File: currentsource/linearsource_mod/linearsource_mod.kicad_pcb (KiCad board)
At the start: 2 copper layers, 50 x 20 mm, 16 parts, among them P1 CONN_01X04, P2 CONN_01X04, Q1 Q_NMOS_DGS, Q2 BC849, U1 LM358

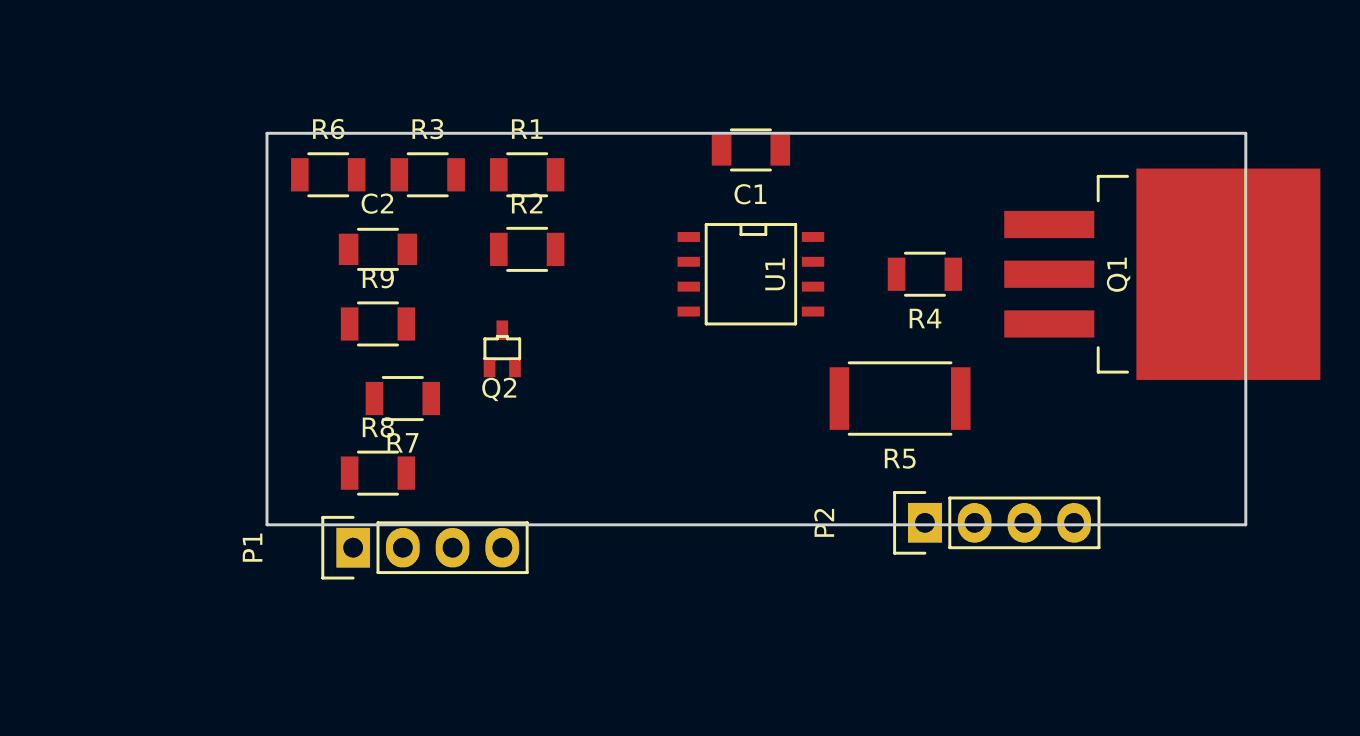
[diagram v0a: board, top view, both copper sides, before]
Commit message: currentsource: Prettify schematic for v2
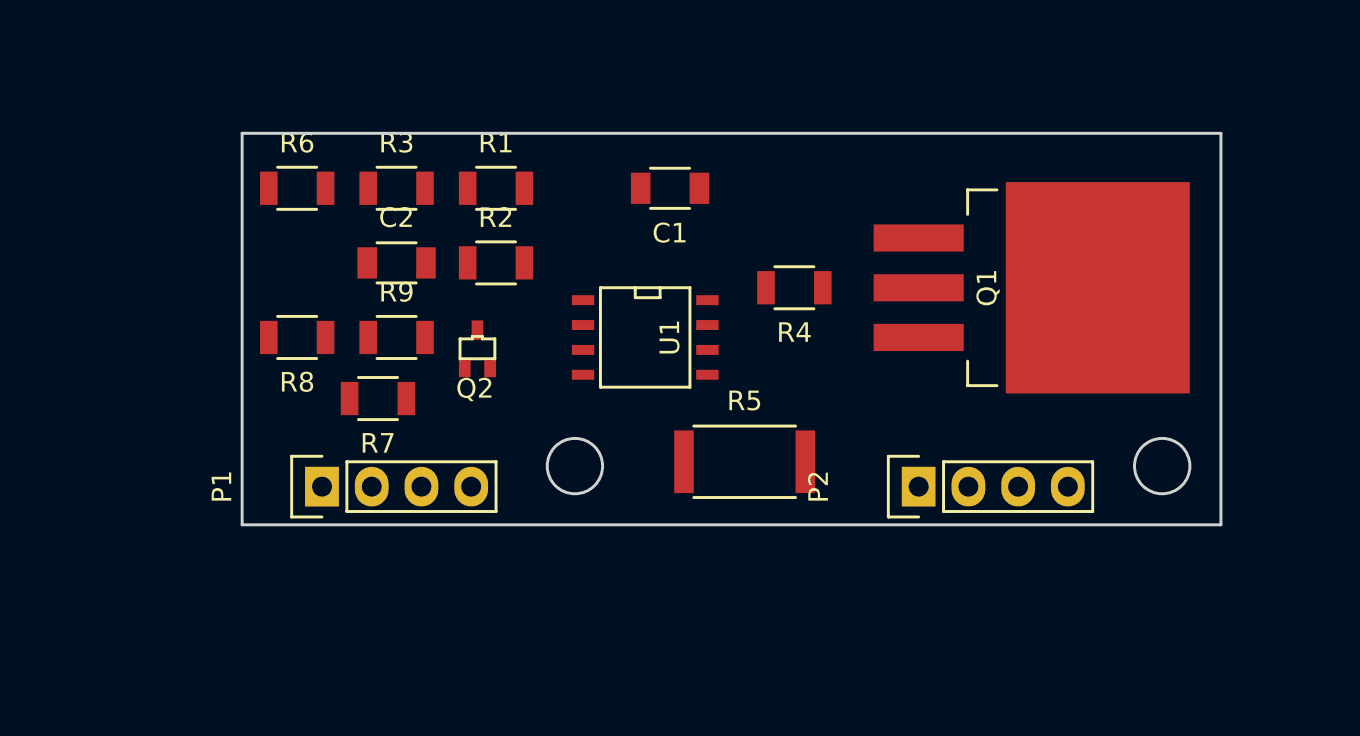
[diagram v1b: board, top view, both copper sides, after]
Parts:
- moved R5 8.57 mm to (172.4, 85.8), turned to 0 degrees
- moved R8 8.07 mm to (149.5, 79.4), turned to 180 degrees
- moved Q1 6.71 mm to (181.3, 76.9)
- moved R4 6.71 mm to (174.9, 76.9)
- moved U1 6.29 mm to (167.3, 79.4)
- moved C1 4.57 mm to (168.6, 71.8)
- moved P1 3.50 mm to (150.8, 87.0)
- moved P2 1.88 mm to (181.3, 87.0)
- moved R1 1.73 mm to (159.7, 71.8)
- moved R2 1.73 mm to (159.7, 75.6)
- moved R3 1.73 mm to (154.6, 71.8)
- moved R6 1.73 mm to (149.5, 71.8)
- moved Q2 1.27 mm to (158.8, 80.0)
- moved R7 1.27 mm to (153.7, 82.5)
- moved R9 1.17 mm to (154.6, 79.4)
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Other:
- outline, holes or cut-outs redrawn
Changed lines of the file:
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@@
     (links 28)
     (no_connects 28)
-    (area 147.924999 68.924999 198.075001 89.075001)
+    (area 146.654999 68.924999 196.805001 89.075001)
     (thickness 1.6)
-    (drawings 4)
+    (drawings 8)
     (tracks 0)
     (zones 0)
@@
     (pad_drill 0.762)
     (pad_to_mask_clearance 0.2)
-    (aux_axis_origin 0 0)
-    (grid_origin 147 68)
+    (aux_axis_origin 145.73 68)
+    (grid_origin 145.73 68)
     (visible_elements FFFEFF7F)
     (pcbplotparams
@@
   )
   (module TO_SOT_Packages_SMD:SOT-323 (layer F.Cu)
-    (at 160.02 80.01 180)
+    (at 158.75 80.01 180)
     (tags "SMD SOT")
     (attr smd)
@@
   )
   (module Capacitors_SMD:C_1206 (layer F.Cu)
-    (at 172.72 69.85 180)
+    (at 168.59 71.81 180)
     (descr "Capacitor SMD 1206, reflow soldering, AVX (see smccp.pdf)")
     (tags "capacitor 1206")
@@
   )
   (module Capacitors_SMD:C_1206 (layer F.Cu)
-    (at 153.67 74.93)
+    (at 154.62 75.62)
     (descr "Capacitor SMD 1206, reflow soldering, AVX (see smccp.pdf)")
     (tags "capacitor 1206")
@@
   )
   (module Pin_Headers:Pin_Header_Straight_1x04 (layer F.Cu)
-    (at 152.4 90.17 90)
+    (at 150.81 87.05 90)
     (descr "Through hole pin header")
     (tags "pin header")
@@
   )
   (module Pin_Headers:Pin_Header_Straight_1x04 (layer F.Cu)
-    (at 181.61 88.9 90)
+    (at 181.29 87.05 90)
     (descr "Through hole pin header")
     (tags "pin header")
@@
   )
   (module TO_SOT_Packages_SMD:TO-263-3Lead (layer F.Cu)
-    (at 187.96 76.2)
+    (at 181.29 76.89)
     (descr "D2PAK / TO-263 3-lead smd package")
     (tags "D2PAK D2PAK-3 TO-263AB TO-263")
@@
   )
   (module Resistors_SMD:R_1206 (layer F.Cu)
-    (at 161.29 71.12)
+    (at 159.7 71.81)
     (descr "Resistor SMD 1206, reflow soldering, Vishay (see dcrcw.pdf)")
     (tags "resistor 1206")
@@
   )
   (module Resistors_SMD:R_1206 (layer F.Cu)
-    (at 161.29 74.93)
+    (at 159.7 75.62)
     (descr "Resistor SMD 1206, reflow soldering, Vishay (see dcrcw.pdf)")
     (tags "resistor 1206")
@@
   )
   (module Resistors_SMD:R_1206 (layer F.Cu)
-    (at 156.21 71.12)
+    (at 154.62 71.81)
     (descr "Resistor SMD 1206, reflow soldering, Vishay (see dcrcw.pdf)")
     (tags "resistor 1206")
@@
   )
   (module Resistors_SMD:R_1206 (layer F.Cu)
-    (at 181.61 76.2 180)
+    (at 174.94 76.89 180)
     (descr "Resistor SMD 1206, reflow soldering, Vishay (see dcrcw.pdf)")
     (tags "resistor 1206")
@@
   )
   (module Resistors_SMD:R_1206 (layer F.Cu)
-    (at 151.13 71.12)
+    (at 149.54 71.81)
     (descr "Resistor SMD 1206, reflow soldering, Vishay (see dcrcw.pdf)")
     (tags "resistor 1206")
@@
   )
   (module Resistors_SMD:R_1206 (layer F.Cu)
-    (at 154.94 82.55 180)
+    (at 153.67 82.55 180)
     (descr "Resistor SMD 1206, reflow soldering, Vishay (see dcrcw.pdf)")
     (tags "resistor 1206")
@@
   )
   (module Resistors_SMD:R_1206 (layer F.Cu)
-    (at 153.67 86.36)
-    (descr "Resistor SMD 1206, reflow soldering, Vishay (see dcrcw.pdf)")
-    (tags "resistor 1206")
-    (attr smd)
-    (fp_text reference R8 (at 0 -2.3) (layer F.SilkS)
-      (effects (font (size 1 1) (thickness 0.15)))
-    )
-    (fp_text value 100k (at 0 2.3) (layer F.Fab)
-      (effects (font (size 1 1) (thickness 0.15)))
-    )
-    (fp_line (start -2.2 -1.2) (end 2.2 -1.2) (layer F.CrtYd) (width 0.05))
-    (fp_line (start -2.2 1.2) (end 2.2 1.2) (layer F.CrtYd) (width 0.05))
-    (fp_line (start -2.2 -1.2) (end -2.2 1.2) (layer F.CrtYd) (width 0.05))
-    (fp_line (start 2.2 -1.2) (end 2.2 1.2) (layer F.CrtYd) (width 0.05))
-    (fp_line (start 1 1.075) (end -1 1.075) (layer F.SilkS) (width 0.15))
-    (fp_line (start -1 -1.075) (end 1 -1.075) (layer F.SilkS) (width 0.15))
-    (pad 1 smd rect (at -1.45 0) (size 0.9 1.7) (layers F.Cu F.Paste F.Mask)
+    (at 149.54 79.43 180)
+    (descr "Resistor SMD 1206, reflow soldering, Vishay (see dcrcw.pdf)")
+    (tags "resistor 1206")
+    (attr smd)
+    (fp_text reference R8 (at 0 -2.3 180) (layer F.SilkS)
+      (effects (font (size 1 1) (thickness 0.15)))
+    )
+    (fp_text value 100k (at 0 2.3 180) (layer F.Fab)
+      (effects (font (size 1 1) (thickness 0.15)))
+    )
+    (fp_line (start -2.2 -1.2) (end 2.2 -1.2) (layer F.CrtYd) (width 0.05))
+    (fp_line (start -2.2 1.2) (end 2.2 1.2) (layer F.CrtYd) (width 0.05))
+    (fp_line (start -2.2 -1.2) (end -2.2 1.2) (layer F.CrtYd) (width 0.05))
+    (fp_line (start 2.2 -1.2) (end 2.2 1.2) (layer F.CrtYd) (width 0.05))
+    (fp_line (start 1 1.075) (end -1 1.075) (layer F.SilkS) (width 0.15))
+    (fp_line (start -1 -1.075) (end 1 -1.075) (layer F.SilkS) (width 0.15))
+    (pad 1 smd rect (at -1.45 0 180) (size 0.9 1.7) (layers F.Cu F.Paste F.Mask)
       (net 5 /I_target))
-    (pad 2 smd rect (at 1.45 0) (size 0.9 1.7) (layers F.Cu F.Paste F.Mask)
+    (pad 2 smd rect (at 1.45 0 180) (size 0.9 1.7) (layers F.Cu F.Paste F.Mask)
       (net 7 I_set))
     (model Resistors_SMD.3dshapes/R_1206.wrl
@@
   )
   (module Resistors_SMD:R_1206 (layer F.Cu)
-    (at 153.67 78.74)
+    (at 154.62 79.43)
     (descr "Resistor SMD 1206, reflow soldering, Vishay (see dcrcw.pdf)")
     (tags "resistor 1206")
@@
   )
   (module SMD_Packages:SOIC-8-N (layer F.Cu)
-    (at 172.72 76.2 270)
+    (at 167.32 79.43 270)
     (descr "Module Narrow CMS SOJ 8 pins large")
     (tags "CMS SOJ")
@@
   )
   (module Resistors_SMD:R_2512 (layer F.Cu)
-    (at 180.34 82.55 180)
+    (at 172.4 85.78)
     (descr "Resistor SMD 2512, reflow soldering, Vishay (see dcrcw.pdf)")
     (tags "resistor 2512")
     (attr smd)
-    (fp_text reference R5 (at 0 -3.1 180) (layer F.SilkS)
-      (effects (font (size 1 1) (thickness 0.15)))
-    )
-    (fp_text value 0.1 (at 0 3.1 180) (layer F.Fab)
+    (fp_text reference R5 (at 0 -3.1) (layer F.SilkS)
+      (effects (font (size 1 1) (thickness 0.15)))
+    )
+    (fp_text value 0.1 (at 0 3.1) (layer F.Fab)
       (effects (font (size 1 1) (thickness 0.15)))
     )
@@
     (fp_line (start 2.6 1.825) (end -2.6 1.825) (layer F.SilkS) (width 0.15))
     (fp_line (start -2.6 -1.825) (end 2.6 -1.825) (layer F.SilkS) (width 0.15))
-    (pad 1 smd rect (at -3.1 0 180) (size 1 3.2) (layers F.Cu F.Paste F.Mask)
+    (pad 1 smd rect (at -3.1 0) (size 1 3.2) (layers F.Cu F.Paste F.Mask)
       (net 12 I_sense))
-    (pad 2 smd rect (at 3.1 0 180) (size 1 3.2) (layers F.Cu F.Paste F.Mask)
+    (pad 2 smd rect (at 3.1 0) (size 1 3.2) (layers F.Cu F.Paste F.Mask)
       (net 8 GNDPWR))
     (model Resistors_SMD.3dshapes/R_2512.wrl
@@
     )
   )
-  (gr_line (start 148 89) (end 148 69) (angle 90) (layer Edge.Cuts) (width 0.15))
-  (gr_line (start 198 89) (end 148 89) (angle 90) (layer Edge.Cuts) (width 0.15))
-  (gr_line (start 198 69) (end 198 89) (angle 90) (layer Edge.Cuts) (width 0.15))
-  (gr_line (start 148 69) (end 198 69) (angle 90) (layer Edge.Cuts) (width 0.15))
+  (gr_circle (center 193.73 86) (end 194.73 85) (layer Edge.Cuts) (width 0.15))
+  (gr_circle (center 163.73 86) (end 164.73 85) (layer Edge.Cuts) (width 0.15))
+  (dimension 20 (width 0.3) (layer Eco2.User)
+    (gr_text "20.000 mm" (at 206.08 79 90) (layer Eco2.User)
+      (effects (font (size 1.5 1.5) (thickness 0.3)))
+    )
+    (feature1 (pts (xy 197.73 69) (xy 207.43 69)))
+    (feature2 (pts (xy 197.73 89) (xy 207.43 89)))
+    (crossbar (pts (xy 204.73 89) (xy 204.73 69)))
+    (arrow1a (pts (xy 204.73 69) (xy 205.316421 70.126504)))
+    (arrow1b (pts (xy 204.73 69) (xy 204.143579 70.126504)))
+    (arrow2a (pts (xy 204.73 89) (xy 205.316421 87.873496)))
+    (arrow2b (pts (xy 204.73 89) (xy 204.143579 87.873496)))
+  )
+  (dimension 50 (width 0.3) (layer Eco2.User)
+    (gr_text "50.000 mm" (at 171.73 95.35) (layer Eco2.User)
+      (effects (font (size 1.5 1.5) (thickness 0.3)))
+    )
+    (feature1 (pts (xy 146.73 90) (xy 146.73 96.7)))
+    (feature2 (pts (xy 196.73 90) (xy 196.73 96.7)))
+    (crossbar (pts (xy 196.73 94) (xy 146.73 94)))
+    (arrow1a (pts (xy 146.73 94) (xy 147.856504 93.413579)))
+    (arrow1b (pts (xy 146.73 94) (xy 147.856504 94.586421)))
+    (arrow2a (pts (xy 196.73 94) (xy 195.603496 93.413579)))
+    (arrow2b (pts (xy 196.73 94) (xy 195.603496 94.586421)))
+  )
+  (gr_line (start 146.73 89) (end 146.73 69) (angle 90) (layer Edge.Cuts) (width 0.15))
+  (gr_line (start 196.73 89) (end 146.73 89) (angle 90) (layer Edge.Cuts) (width 0.15))
+  (gr_line (start 196.73 69) (end 196.73 89) (angle 90) (layer Edge.Cuts) (width 0.15))
+  (gr_line (start 146.73 69) (end 196.73 69) (angle 90) (layer Edge.Cuts) (width 0.15))
 )

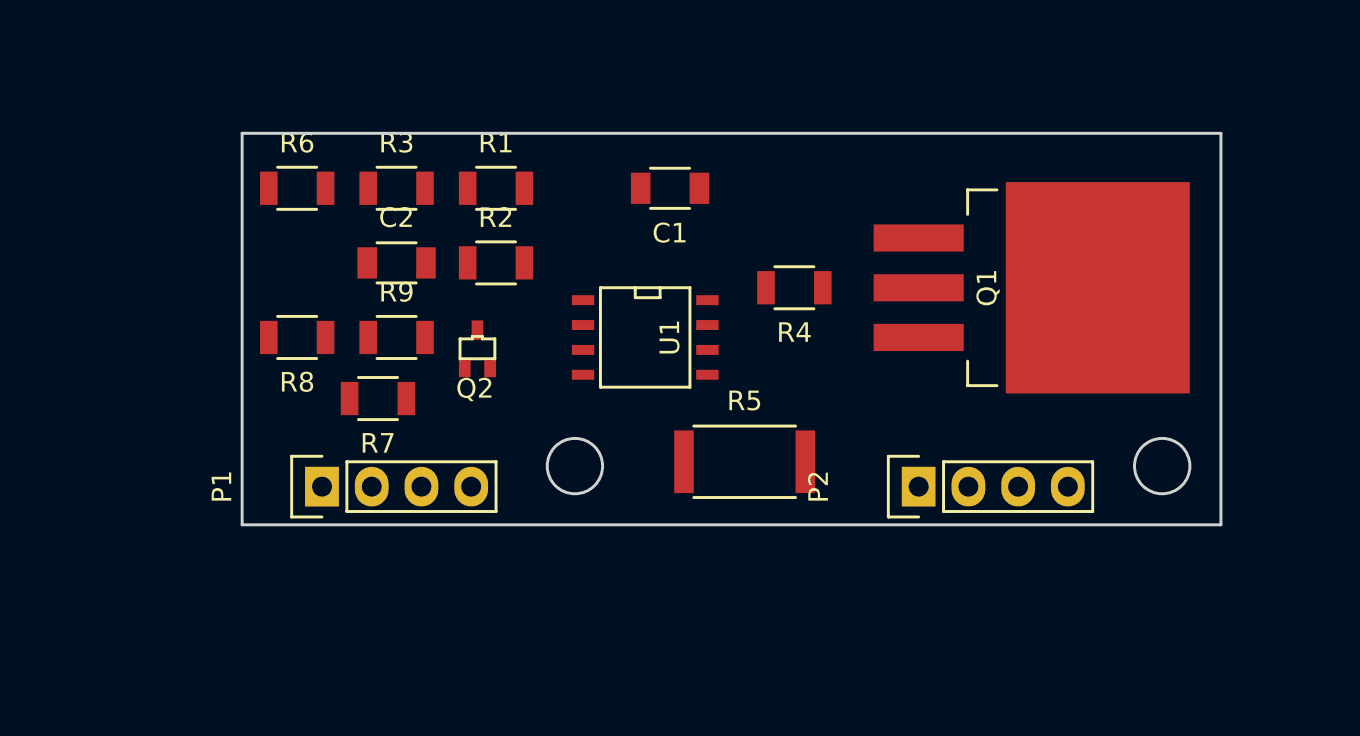
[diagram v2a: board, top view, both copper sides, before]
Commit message: currentsource: Start of routing tracks
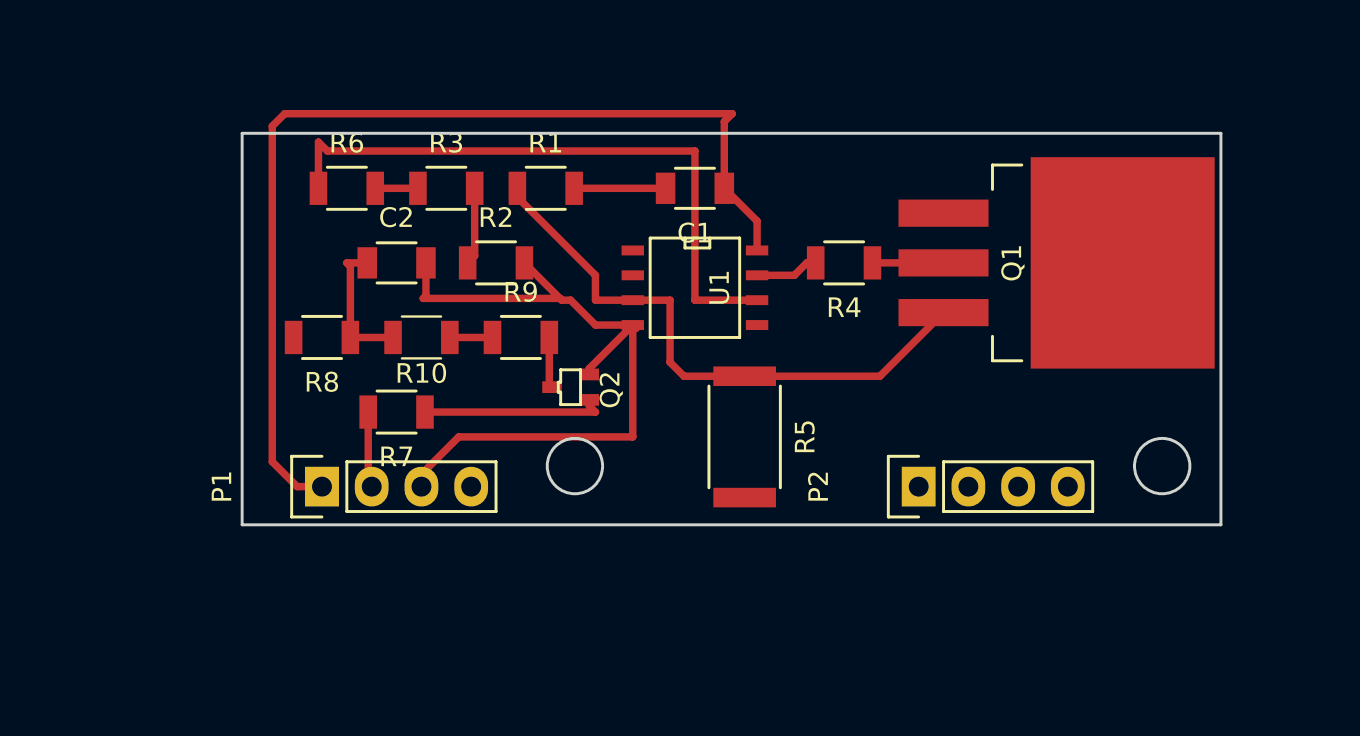
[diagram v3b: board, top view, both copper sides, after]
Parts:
- added R10: 100k, Resistors_SMD:R_1206, F.Cu at (155.9, 79.4)
- Q1: value Q_NMOS_DGS -> PSMN017-30BL
- moved R9 6.35 mm to (161.0, 79.4)
- moved Q2 5.15 mm to (163.5, 82.0), turned to 270 degrees
- moved U1 3.59 mm to (169.9, 76.9)
- moved R4 2.84 mm to (177.5, 75.6)
- moved R1 2.54 mm to (162.2, 71.8)
- moved R6 2.54 mm to (152.1, 71.8)
- moved R3 2.54 mm to (157.2, 71.8)
- moved Q1 1.80 mm to (182.6, 75.6)
- moved C1 1.27 mm to (169.9, 71.8)
- moved R8 1.27 mm to (150.8, 79.4)
- moved R5 1.27 mm to (172.4, 84.5), turned to 270 degrees
- moved R7 1.17 mm to (154.6, 83.2)
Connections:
- C2 pad 1: /I_target -> Net-(C2-Pad1)
- P2 pad 1: GNDPWR -> GND
- R5 pad 2: GNDPWR -> GND
- R8 pad 1: /I_target -> Net-(C2-Pad1)
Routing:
- net VCC: track 0.00 -> 51.8 mm
- net GND: track 0.00 -> 42.0 mm
- net /I_feedback: track 0.00 -> 32.6 mm
- net I_sense: track 0.00 -> 30.0 mm
- net Net-(Q2-Pad1): track 0.00 -> 9.46 mm
- net Net-(C2-Pad1): track 0.00 -> 7.10 mm
- net Net-(R2-Pad1): track 0.00 -> 3.96 mm
- net PWM: track 0.00 -> 3.88 mm
- net Net-(Q1-Pad2): track 0.00 -> 3.63 mm
- net Net-(R4-Pad2): track 0.00 -> 3.26 mm
- net Net-(Q2-Pad3): track 0.00 -> 2.60 mm
- net Net-(R3-Pad1): track 0.00 -> 2.18 mm
- net /I_target: track 0.00 -> 2.18 mm
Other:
- net class Default: clearance 0.2 -> 0.381; trace_width 0.25 -> 0.381; via_dia 0.6 -> 1; via_drill 0.4 -> 0.01
- rule trace_clearance: 0.2 -> 0.381
- rule via_min_drill: 0.3 -> 0.01

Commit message: currentsource: Basic layout done
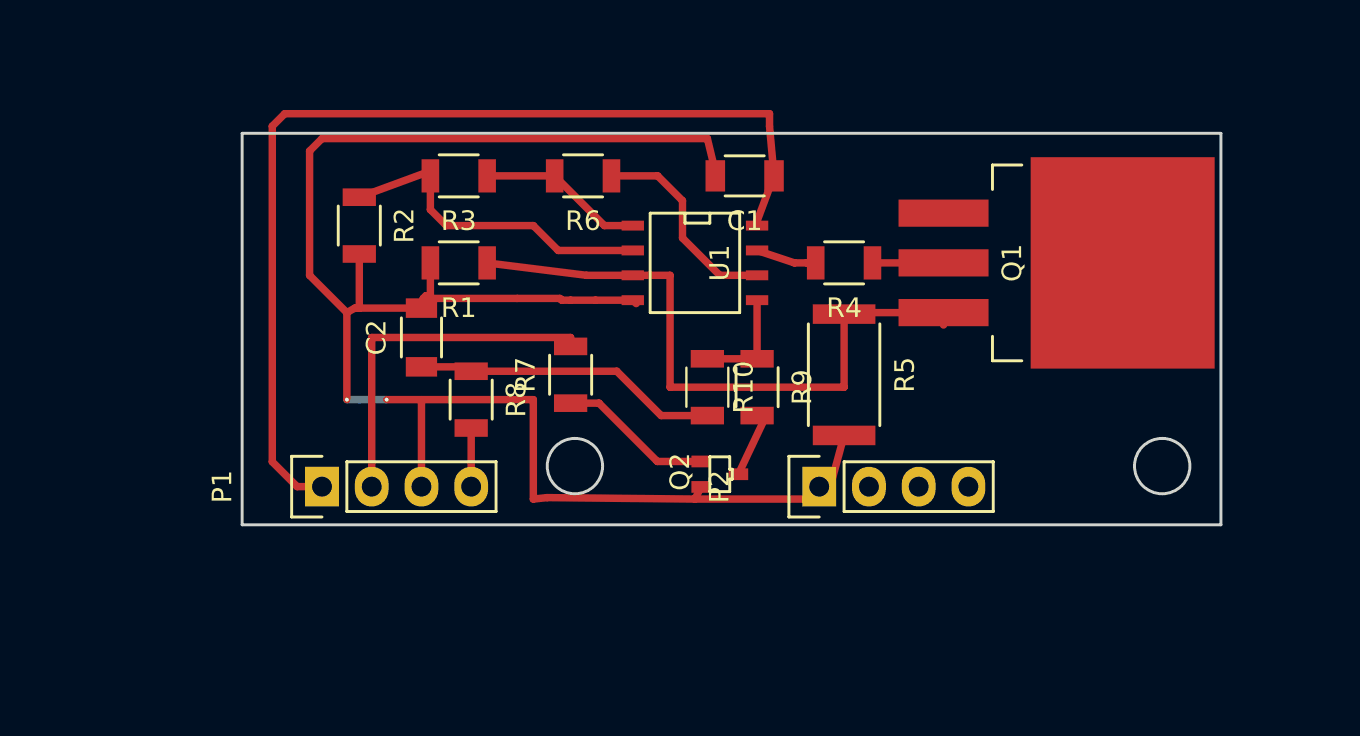
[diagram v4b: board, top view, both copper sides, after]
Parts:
- moved R10 14.8 mm to (170.5, 82.0), turned to 270 degrees
- moved R9 12.3 mm to (173.0, 82.0), turned to 270 degrees
- moved R6 12.1 mm to (164.1, 71.2), turned to 180 degrees
- moved R7 9.09 mm to (163.5, 81.3), turned to 90 degrees
- moved Q2 8.82 mm to (171.1, 86.4), turned to 90 degrees
- moved R8 8.26 mm to (158.4, 82.6), turned to 270 degrees
- moved R2 7.24 mm to (152.7, 73.7), turned to 270 degrees
- moved R5 5.99 mm to (177.5, 81.3)
- moved R1 5.85 mm to (157.8, 75.6), turned to 180 degrees
- moved P2 5.08 mm to (176.2, 87.0)
- moved C2 4.02 mm to (155.9, 79.4), turned to 90 degrees
- moved C1 2.62 mm to (172.4, 71.2)
- moved U1 1.27 mm to (169.9, 75.6)
- moved R3 0.90 mm to (157.8, 71.2), turned to 180 degrees
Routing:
- net GND: track 42.0 -> 95.6 mm, vias 0 -> 2
- net /I_feedback: track 32.6 -> 10.7 mm
- net PWM: track 3.88 -> 18.3 mm
- net Net-(R2-Pad1): track 3.96 -> 16.9 mm
- net Net-(C2-Pad1): track 7.10 -> 15.6 mm
- net Net-(R3-Pad1): track 2.18 -> 8.49 mm
- net I_sense: track 30.0 -> 33.4 mm
- net /I_target: track 2.18 -> 5.53 mm
- net I_set: track 0.00 -> 2.99 mm
- net Net-(Q2-Pad1): track 9.46 -> 7.90 mm
- net Net-(Q2-Pad3): track 2.60 -> 3.41 mm
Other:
- net class Default: via_dia 1 -> 0.2
- rule via_min_size: 0.4 -> 0.1
